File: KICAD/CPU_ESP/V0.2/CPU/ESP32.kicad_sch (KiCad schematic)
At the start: 30 parts, among them U401 ESP32-WROOM-32, U402 FT232RL, U403 TJA1051T

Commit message: KICAD MAJOR UPDATE V0.2
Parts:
- added Q401: BC817, Package_TO_SOT_SMD:SOT-23, symbol Transistor_BJT:BC817
- added Q402: BC807, Package_TO_SOT_SMD:SOT-23, symbol Transistor_BJT:BC807
- added R415, R416: 10k, Resistor_SMD:R_0603_1608Metric, symbol Device:R
- R405: value NC -> 0
- R408, R409: value 4k7 -> 330
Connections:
- net BOOT: now also Q402.2 (E)
- net RESET: now also Q401.3 (C); no longer R404.2
- net T2CK: now also U401.7 (IO35); no longer U401.29 (IO5)
- net DTR: now reaches R405.2
- net DTR: now also Q402.3 (C), R415.1
- net at R413.2: now also U401.29 (IO5); no longer U401.7 (IO35)
- new net: Q401.1 (B), R415.2
- new net: Q402.1 (B), R416.2
- new net RTS: Q401.2 (E), R404.2, R416.1
- no-connect marks 10 -> 9
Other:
- note added: "IO34&IO35 READ ONLY"
- note added: "ROUGE"
- note added: "VERT"

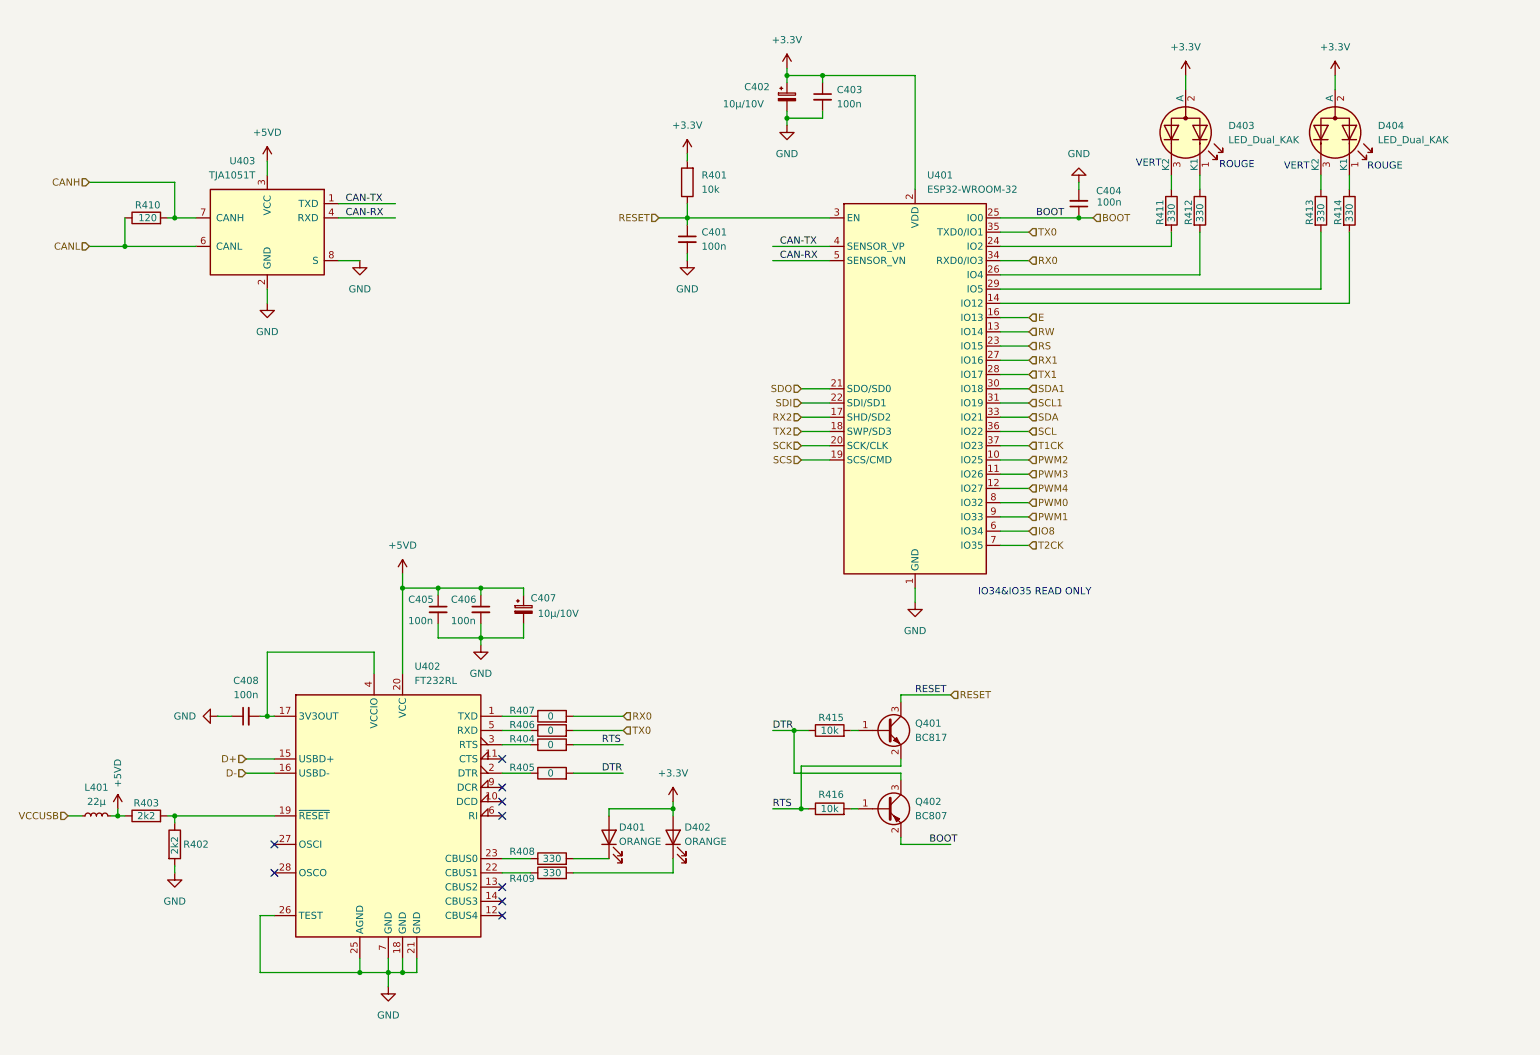
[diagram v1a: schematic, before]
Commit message: KICAD 4 UART update
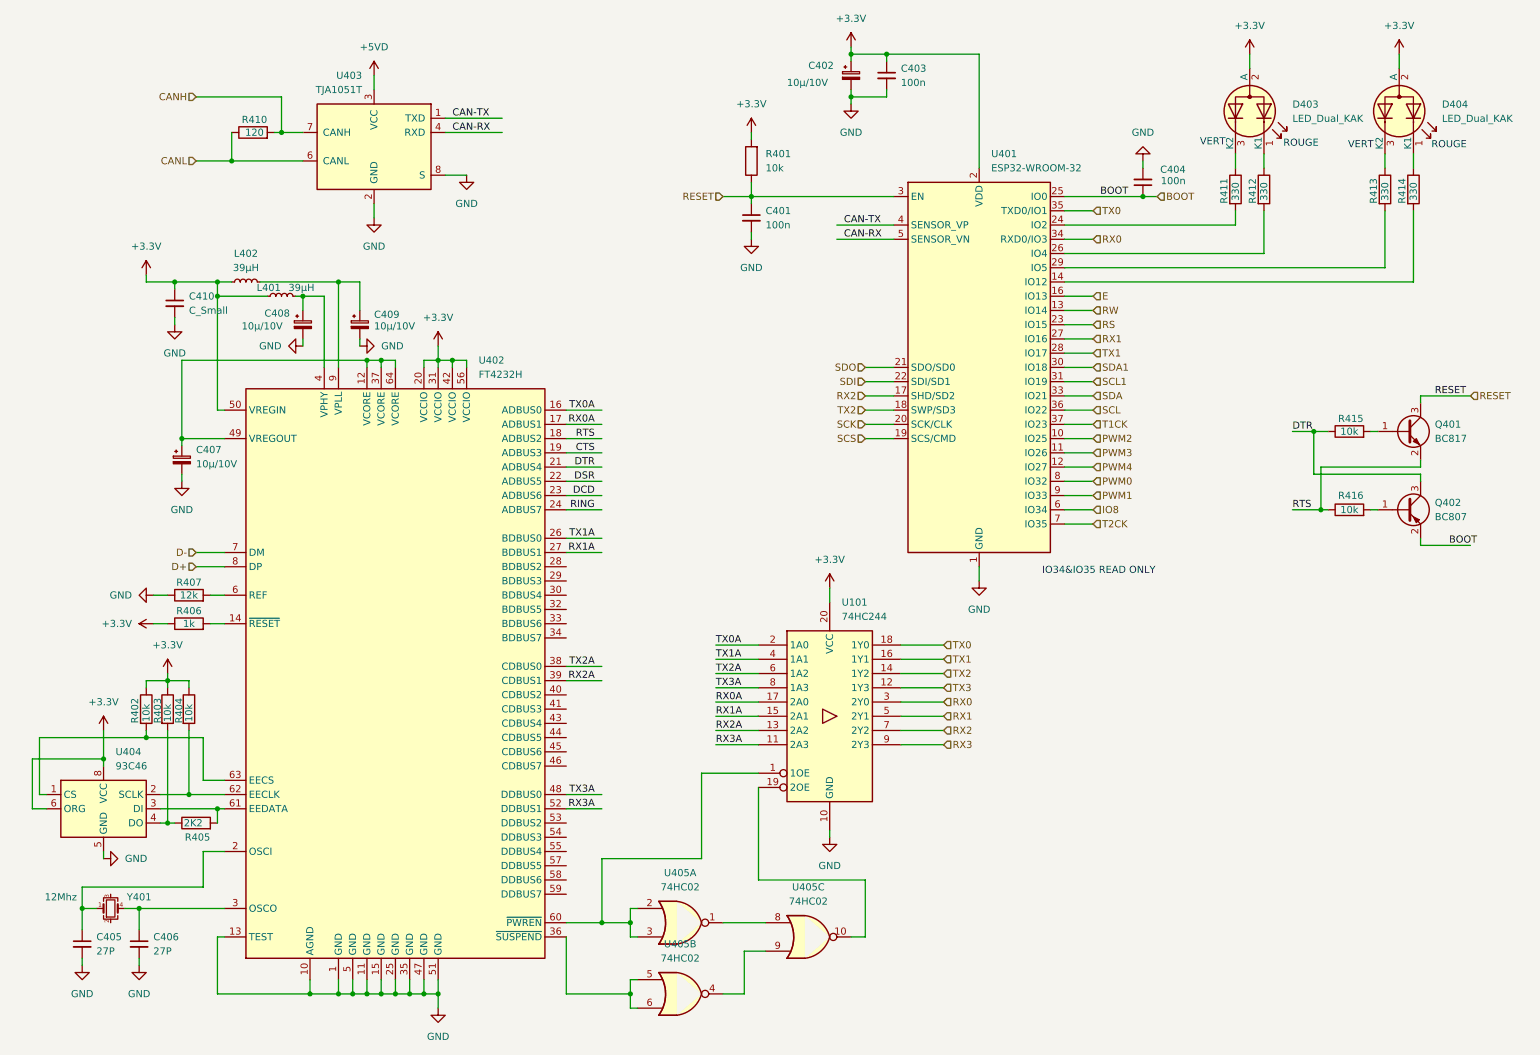
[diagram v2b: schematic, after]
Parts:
- removed C408: 100n, Capacitor_SMD:C_0603_1608Metric, symbol Device:C_Small
- removed D401, D402: ORANGE, LED_SMD:LED_0603_1608Metric, symbol Device:LED
- removed R408, R409: 330, Resistor_SMD:R_0603_1608Metric, symbol Device:R
- removed U402: FT232RL, Package_SO:SSOP-28_5.3x10.2mm_P0.65mm, symbol Interface_USB:FT232RL
- added C408, C409: 10µ/10V, Capacitor_Tantalum_SMD:CP_EIA-3216-12_Kemet-S_HandSolder, symbol Device:C_Polarized_Small
- added C410: C_Small, symbol Device:C_Small
- added L402: 39µH, symbol Device:L_Small
- added U101: 74HC244, symbol 74xx:74HC244
- added U402: FT4232H, symbol Interface_USB:FT4232H
- added U404: 93C46, symbol Memory_EEPROM:93CxxC
- added U405: 74HC02, symbol 74xx:74HC02
- added Y401: 12Mhz, symbol Device:Crystal_GND23_Small
- C405, C406: value 100n -> 27P
- C407: footprint Capacitor_Tantalum_SMD:CP_EIA-3216-12_Kemet-S -> Capacitor_Tantalum_SMD:CP_EIA-3216-12_Kemet-S_HandSolder
- L401: value 22µ -> 39µH; footprint Inductor_SMD:L_1008_2520Metric -> (none)
- R402, R403: value 2k2 -> 10k; footprint Resistor_SMD:R_0603_1608Metric -> Resistor_SMD:R_0603_1608Metric_Pad0.98x0.95mm_HandSolder
- R404: value 0 -> 10k; footprint Resistor_SMD:R_0603_1608Metric -> Resistor_SMD:R_0603_1608Metric_Pad0.98x0.95mm_HandSolder
- R405: value 0 -> 2K2; footprint Resistor_SMD:R_0603_1608Metric -> Resistor_SMD:R_0603_1608Metric_Pad0.98x0.95mm_HandSolder
- R406: value 0 -> 1k; footprint Resistor_SMD:R_0603_1608Metric -> (none)
- R407: value 0 -> 12k; footprint Resistor_SMD:R_0603_1608Metric -> (none)
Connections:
- net VCCUSB is gone; now on net +3.3V: L401.1
- net +3.3V: now also R402.1, R403.1, R404.1, R406.1, C410.1, L402.1, U101.20 (VCC), U402.20 (VCCIO), U402.31 (VCCIO), U402.42 (VCCIO), U402.50 (VREGIN), U402.56 (VCCIO), U404.6 (ORG), U404.8 (VCC)
- net +5VD: no longer C405.1, C406.1, C407.1, L401.2, R403.1
- net D+: now also U402.8 (DP)
- net D-: now also U402.7 (DM)
- net DTR: now also U402.21 (ADBUS4); no longer R405.2
- net GND: now also R407.1, C408.2, C409.2, C410.2, U101.10 (GND), U402.1 (GND), U402.10 (AGND), U402.11 (GND), U402.13 (TEST), U402.15 (GND), U402.25 (GND), U402.35 (GND), U402.47 (GND), U402.5 (GND), U402.51 (GND), U404.5 (GND); no longer R402.2
- net RTS: now also U402.18 (ADBUS2); no longer R404.2
- net RX0: now also U101.3 (2Y0); no longer R407.2
- net RX1: now also U101.5 (2Y1)
- net RX2: now also U101.7 (2Y2)
- net TX0: now also U101.18 (1Y0); no longer R406.2
- net TX1: now also U101.16 (1Y1)
- net TX2: now also U101.14 (1Y2)
- net at R403.2: now also R405.1, U404.4 (DO); no longer R402.1
- new net: C409.1, L402.2, U402.9 (VPLL)
- new net: R404.2, U402.62 (EECLK), U404.2 (SCLK)
- new net: U101.19 (2OE), U405.10
- new net: U405.1, U405.8
- new net: U405.4, U405.9
- new net: C405.1, U402.2 (OSCI), Y401.1
- new net: C406.1, U402.3 (OSCO), Y401.4
- new net: R402.2, U402.63 (EECS), U404.1 (CS)
- new net: C407.1, U402.12 (VCORE), U402.37 (VCORE), U402.49 (VREGOUT), U402.64 (VCORE)
- new net: R406.2, U402.14 (~{RESET})
- new net: U402.36 (~{SUSPEND}), U405.5, U405.6
- new net: C408.1, L401.2, U402.4 (VPHY)
- new net: R407.2, U402.6 (REF)
- new net: U101.1 (1OE), U402.60 (~{PWREN}), U405.2, U405.3
- new net: R405.2, U402.61 (EEDATA), U404.3 (DI)
- new net CTS: U402.19 (ADBUS3)
- new net DCD: U402.23 (ADBUS6)
- new net DSR: U402.22 (ADBUS5)
- new net RING: U402.24 (ADBUS7)
- new net RX0A: U101.17 (2A0), U402.17 (ADBUS1)
- new net RX1A: U101.15 (2A1), U402.27 (BDBUS1)
- new net RX2A: U101.13 (2A2), U402.39 (CDBUS1)
- new net RX3: U101.9 (2Y3)
- new net RX3A: U101.11 (2A3), U402.52 (DDBUS1)
- new net TX0A: U101.2 (1A0), U402.16 (ADBUS0)
- new net TX1A: U101.4 (1A1), U402.26 (BDBUS0)
- new net TX2A: U101.6 (1A2), U402.38 (CDBUS0)
- new net TX3: U101.12 (1Y3)
- new net TX3A: U101.8 (1A3), U402.48 (DDBUS0)
- no-connect marks 9 -> 0
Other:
- moved on the sheet: C401, C402, C403, C404, D403, D404, Q401, Q402, R401, R410, R411, R412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

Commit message: KICAD 4 UART update
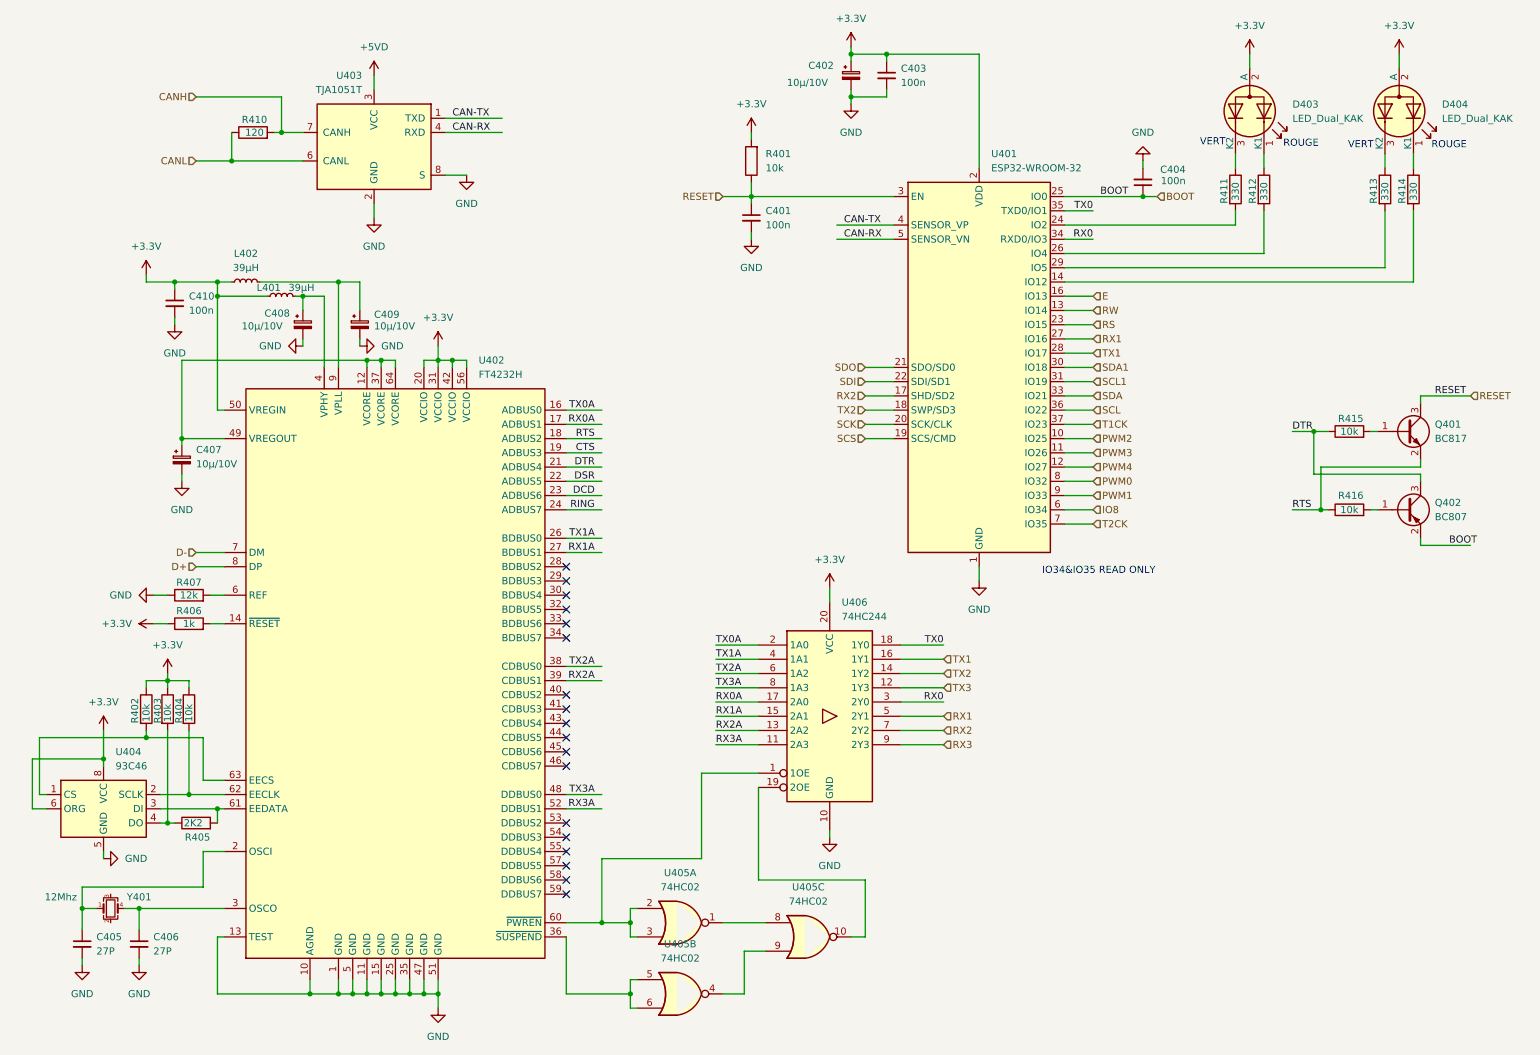
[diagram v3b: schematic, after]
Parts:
- C410: value C_Small -> 100n; footprint (none) -> Capacitor_SMD:C_0603_1608Metric_Pad1.08x0.95mm_HandSolder
- L401, L402: footprint (none) -> Capacitor_SMD:C_2220_5750Metric
- R406, R407: footprint (none) -> Resistor_SMD:R_0603_1608Metric
- U402: footprint (none) -> Package_QFP:TQFP-64_10x10mm_P0.5mm
- U404: footprint (none) -> Package_SO:SOIC-8_5.3x5.3mm_P1.27mm
- U405: footprint (none) -> Package_SO:SOIC-14_3.9x8.7mm_P1.27mm
- U406: renamed from U101; footprint (none) -> Package_SO:TSSOP-20_4.4x5mm_P0.5mm
- Y401: footprint (none) -> Crystal:Crystal_HC49-U_Vertical
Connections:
- no-connect marks 0 -> 18

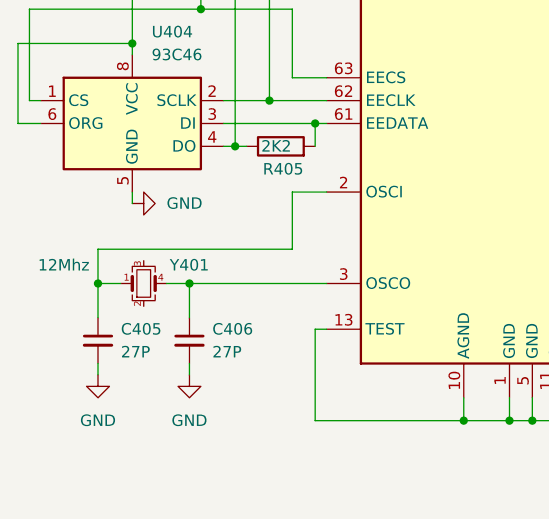
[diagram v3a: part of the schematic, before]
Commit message: KICAD 4 UART update
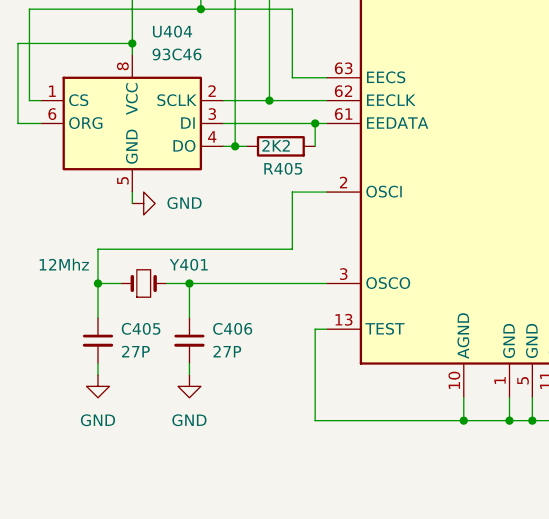
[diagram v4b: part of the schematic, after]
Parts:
- U402: footprint Package_QFP:TQFP-64_10x10mm_P0.5mm -> Package_QFP:LQFP-64_10x10mm_P0.5mm
- Y401: symbol Device:Crystal_GND23_Small -> Device:Crystal_Small
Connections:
- net at Y401.2: now also C406.1, U402.3 (OSCO)
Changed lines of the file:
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@@
 	)
 	(symbol
-		(lib_id "Device:Crystal_GND23_Small")
+		(lib_id "Device:Crystal_Small")
 		(at 31.75 172.72 0)
 		(unit 1)
@@
 			)
 		)
-		(property "Description" "Four pin crystal, GND on pins 2 and 3, small symbol"
+		(property "Description" "Two pin crystal, small symbol"
 			(at 31.75 172.72 0)
 			(effects
@@
 				(hide yes)
 			)
-		)
-		(pin "4"
-		)
-		(pin "3"
 		)
 		(pin "1"
@@
 			)
 		)
-		(property "Footprint" "Package_QFP:TQFP-64_10x10mm_P0.5mm"
+		(property "Footprint" "Package_QFP:LQFP-64_10x10mm_P0.5mm"
 			(at 82.55 132.08 0)
 			(effects
@@
 			(at 82.55 132.08 0)
 			(effects
+				(font
+					(size 1.27 1.27)
+				)
+				(hide yes)
+			)
+		)
+		(property "UART" ""
+			(at 82.55 132.08 0)
+			(effects
